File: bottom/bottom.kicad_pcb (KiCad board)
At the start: 2 copper layers, 27.5 x 37.7 mm, 2 parts, among them P1 HLW4R-2C7LF, P2 CONN_5

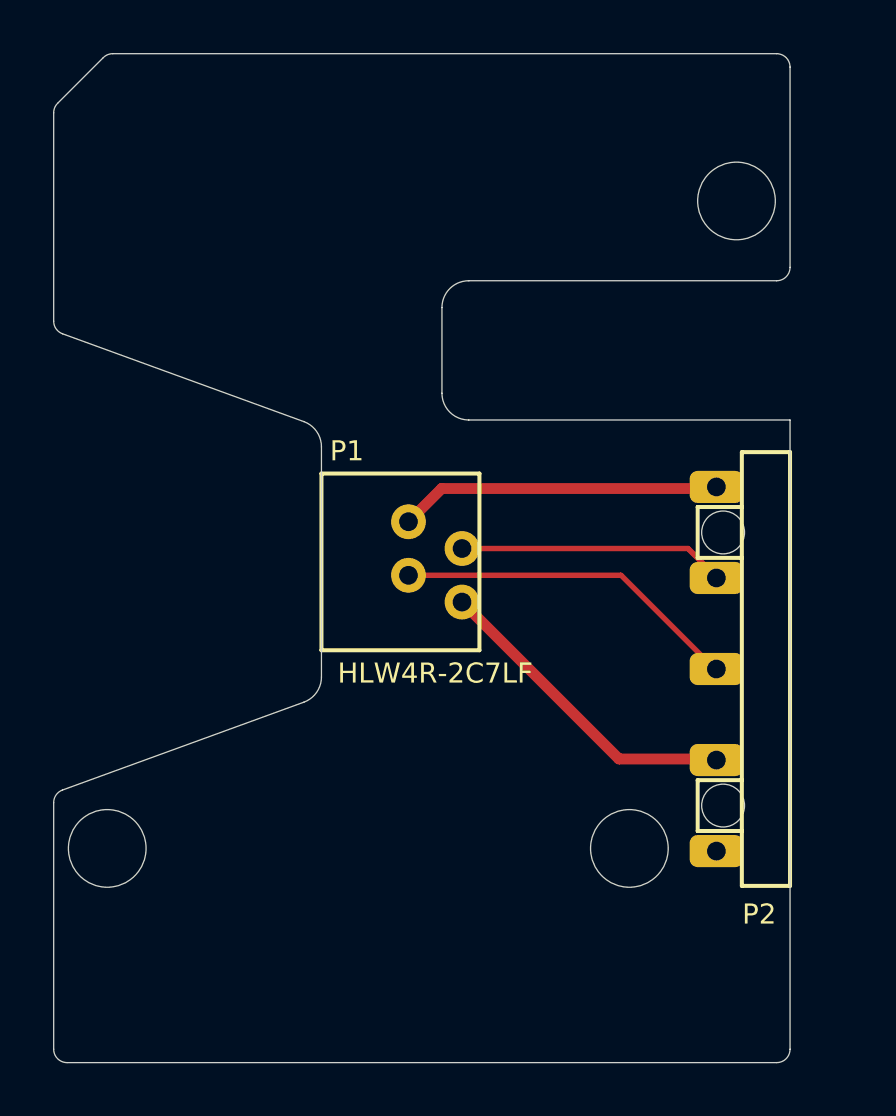
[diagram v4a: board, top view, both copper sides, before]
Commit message: Replace circles with holes.
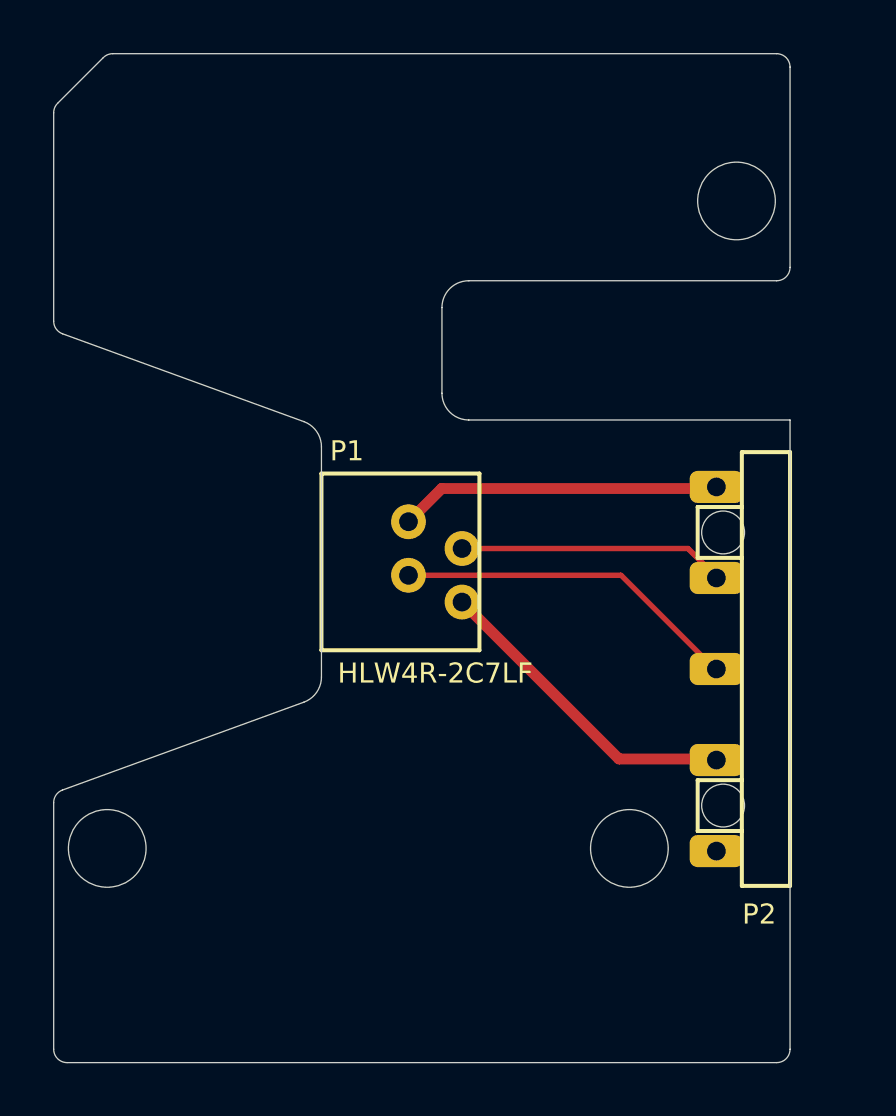
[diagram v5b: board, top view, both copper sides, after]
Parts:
- added ?: , UGL:hole_2.8999999999999773mm, Edge.Cuts at (219.3, 149.8)
- added ?: , UGL:hole_2.8999999999999773mm, Edge.Cuts at (199.8, 149.8)
- added ?: , UGL:hole_2.9000000000000057mm, Edge.Cuts at (223.3, 125.7)
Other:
- outline, holes or cut-outs redrawn
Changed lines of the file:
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@@
   )
   (gr_circle (center 219.35 149.839996) (end 221 149.839996) (layer Eco1.User) (width 0.01))
-  (gr_circle (center 219.35 149.839996) (end 219.35 151.289996) (layer Edge.Cuts) (width 0.01))
+  (module UGL:hole_2.8999999999999773mm locked (layer Edge.Cuts)
+    (at 219.35 149.839996)
+    (attr virtual)
+    (pad "" np_thru_hole circle (at 0 0) (size 2.8999999999999773 2.8999999999999773) (drill 2.8999999999999773) (layers *.Cu *.Mask F.SilkS)
+      (clearance 0.00001)
+    )
+  )
   (gr_circle (center 199.85 149.839996) (end 201.5 149.839996) (layer Eco1.User) (width 0.01))
-  (gr_circle (center 199.85 149.839996) (end 199.85 151.289996) (layer Edge.Cuts) (width 0.01))
+  (module UGL:hole_2.8999999999999773mm locked (layer Edge.Cuts)
+    (at 199.85 149.839996)
+    (attr virtual)
+    (pad "" np_thru_hole circle (at 0 0) (size 2.8999999999999773 2.8999999999999773) (drill 2.8999999999999773) (layers *.Cu *.Mask F.SilkS)
+      (clearance 0.00001)
+    )
+  )
   (gr_circle (center 223.35 125.660004) (end 225 125.660004) (layer Eco1.User) (width 0.01))
-  (gr_circle (center 223.35 125.660004) (end 223.35 127.110004) (layer Edge.Cuts) (width 0.01))
+  (module UGL:hole_2.9000000000000057mm locked (layer Edge.Cuts)
+    (at 223.35 125.660004)
+    (attr virtual)
+    (pad "" np_thru_hole circle (at 0 0) (size 2.9000000000000057 2.9000000000000057) (drill 2.9000000000000057) (layers *.Cu *.Mask F.SilkS)
+      (clearance 0.00001)
+    )
+  )
   (gr_arc (start 198.35 157.339989) (end 197.85 157.34) (angle -89.98521397) (layer Edge.Cuts) (width 0.01))
   (gr_arc (start 198.349992 148.129806) (end 198.17899 147.65996) (angle -70.01492042) (layer Edge.Cuts) (width 0.01))

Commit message: Update description.
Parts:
- ? (x3): moved to F.Cu
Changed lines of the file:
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@@
   (general
     (thickness 1.6)
-    (drawings 32)
+    (drawings 29)
     (tracks 8)
     (zones 0)
-    (modules 2)
+    (modules 5)
     (nets 6)
   )
   (page A3)
   (title_block
-    (title "UHK Touchpad - Bottom")
+    (title "UHK Touchpad Module - Bottom Board")
     (rev 1.0.0)
     (company "Ultimate Gadget Laboratories Kft.")
@@
       (net 1 /VCC) (clearance 0.0762))
   )
+  (module UGL:hole_2.8999999999999773mm locked (layer F.Cu)
+    (at 219.35 149.839996)
+    (attr virtual)
+    (fp_text reference "" (at 0 0) (layer F.SilkS)
+      (effects (font (size 1.27 1.27) (thickness 0.15)))
+    )
+    (fp_text value "" (at 0 0) (layer F.SilkS)
+      (effects (font (size 1.27 1.27) (thickness 0.15)))
+    )
+    (pad "" np_thru_hole circle (at 0 0) (size 2.9 2.9) (drill 2.9) (layers *.Cu *.Mask F.SilkS)
+      (clearance 0.00001))
+  )
+  (module UGL:hole_2.8999999999999773mm locked (layer F.Cu)
+    (at 199.85 149.839996)
+    (attr virtual)
+    (fp_text reference "" (at 0 0) (layer F.SilkS)
+      (effects (font (size 1.27 1.27) (thickness 0.15)))
+    )
+    (fp_text value "" (at 0 0) (layer F.SilkS)
+      (effects (font (size 1.27 1.27) (thickness 0.15)))
+    )
+    (pad "" np_thru_hole circle (at 0 0) (size 2.9 2.9) (drill 2.9) (layers *.Cu *.Mask F.SilkS)
+      (clearance 0.00001))
+  )
+  (module UGL:hole_2.9000000000000057mm locked (layer F.Cu)
+    (at 223.35 125.660004)
+    (attr virtual)
+    (fp_text reference "" (at 0 0) (layer F.SilkS)
+      (effects (font (size 1.27 1.27) (thickness 0.15)))
+    )
+    (fp_text value "" (at 0 0) (layer F.SilkS)
+      (effects (font (size 1.27 1.27) (thickness 0.15)))
+    )
+    (pad "" np_thru_hole circle (at 0 0) (size 2.9 2.9) (drill 2.9) (layers *.Cu *.Mask F.SilkS)
+      (clearance 0.00001))
+  )
   (gr_text "PCB ID: touchpad_bottom_1.0.0" (at 212 156.8) (layer B.SilkS)
     (effects (font (size 0.75 0.75) (thickness 0.15)) (justify mirror))
   )
   (gr_circle (center 219.35 149.839996) (end 221 149.839996) (layer Eco1.User) (width 0.01))
-  (module UGL:hole_2.8999999999999773mm locked (layer Edge.Cuts)
-    (at 219.35 149.839996)
-    (attr virtual)
-    (pad "" np_thru_hole circle (at 0 0) (size 2.8999999999999773 2.8999999999999773) (drill 2.8999999999999773) (layers *.Cu *.Mask F.SilkS)
-      (clearance 0.00001)
-    )
-  )
   (gr_circle (center 199.85 149.839996) (end 201.5 149.839996) (layer Eco1.User) (width 0.01))
-  (module UGL:hole_2.8999999999999773mm locked (layer Edge.Cuts)
-    (at 199.85 149.839996)
-    (attr virtual)
-    (pad "" np_thru_hole circle (at 0 0) (size 2.8999999999999773 2.8999999999999773) (drill 2.8999999999999773) (layers *.Cu *.Mask F.SilkS)
-      (clearance 0.00001)
-    )
-  )
   (gr_circle (center 223.35 125.660004) (end 225 125.660004) (layer Eco1.User) (width 0.01))
-  (module UGL:hole_2.9000000000000057mm locked (layer Edge.Cuts)
-    (at 223.35 125.660004)
-    (attr virtual)
-    (pad "" np_thru_hole circle (at 0 0) (size 2.9000000000000057 2.9000000000000057) (drill 2.9000000000000057) (layers *.Cu *.Mask F.SilkS)
-      (clearance 0.00001)
-    )
-  )
   (gr_arc (start 198.35 157.339989) (end 197.85 157.34) (angle -89.98521397) (layer Edge.Cuts) (width 0.01))
   (gr_arc (start 198.349992 148.129806) (end 198.17899 147.65996) (angle -70.01492042) (layer Edge.Cuts) (width 0.01))

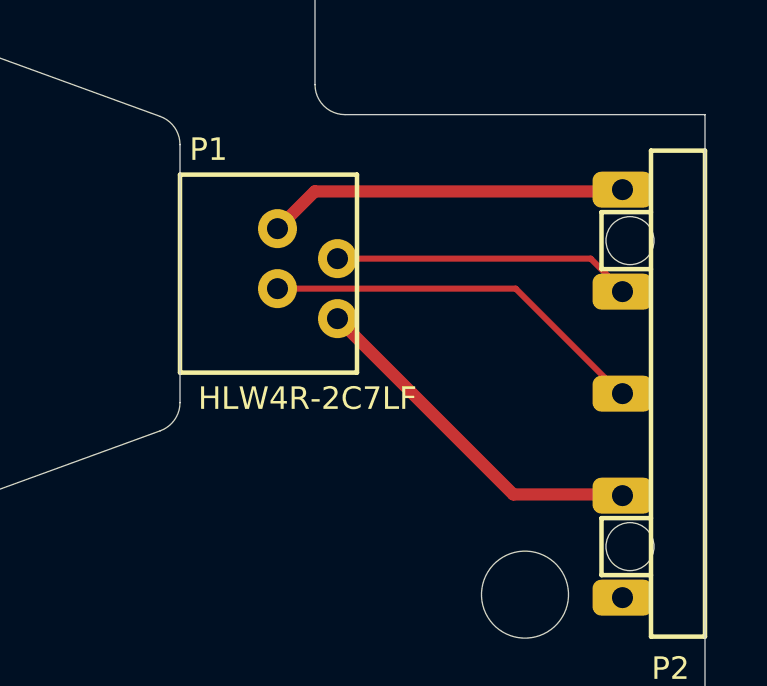
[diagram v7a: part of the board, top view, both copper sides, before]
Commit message: Increase track width on bottom PCB.
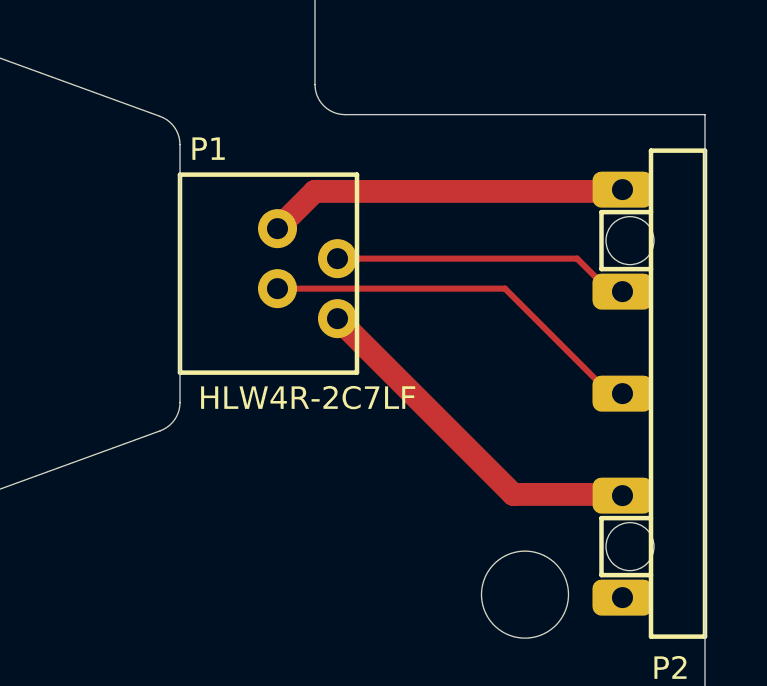
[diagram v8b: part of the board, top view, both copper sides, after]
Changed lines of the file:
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@@
-(kicad_pcb (version 20171130) (host pcbnew 5.1.2-f72e74a~84~ubuntu18.04.1)
+(kicad_pcb (version 20171130) (host pcbnew "(5.0.0)")
   (general
     (thickness 1.6)
     (drawings 33)
-    (tracks 8)
+    (tracks 10)
     (zones 0)
     (modules 5)
@@
   )
   (setup
-    (last_trace_width 0.2032)
+    (last_trace_width 0.4064)
     (user_trace_width 0.4064)
     (trace_clearance 0.2032)
@@
     (zone_45_only no)
     (trace_min 0.2032)
+    (segment_width 0.2)
+    (edge_width 0.1)
     (via_size 0.889)
     (via_drill 0.635)
@@
     (uvia_min_size 0.508)
     (uvia_min_drill 0.127)
-    (edge_width 0.1)
-    (segment_width 0.2)
     (pcb_text_width 0.3)
     (pcb_text_size 1.5 1.5)
@@
     (pad_to_mask_clearance 0)
     (aux_axis_origin 0 0)
-    (visible_elements FFFFEF7F)
+    (visible_elements 7FFFFFFF)
     (pcbplotparams
       (layerselection 0x00030_ffffffff)
@@
     (uvia_dia 0.508)
     (uvia_drill 0.127)
+    (diff_pair_gap 0.25)
     (diff_pair_width 0.2032)
-    (diff_pair_gap 0.25)
     (add_net /GND)
     (add_net /MERGE_SENSE)
@@
   (gr_circle (center 223.35 155.339996) (end 223.35 157.239996) (layer Eco1.User) (width 0.01))
   (gr_arc (start 199.666942 155.331772) (end 197.85 155.948276) (angle -322.8371138) (layer Eco1.User) (width 0.01))
-  (segment (start 211.1 137.639999) (end 212.339999 136.4) (width 0.4064) (layer F.Cu) (net 1))
-  (segment (start 212.339999 136.4) (end 222.6 136.4) (width 0.4064) (layer F.Cu) (net 1))
-  (segment (start 213.1 138.639999) (end 221.539999 138.639999) (width 0.2032) (layer F.Cu) (net 2))
-  (segment (start 221.539999 138.639999) (end 222.6 139.7) (width 0.2032) (layer F.Cu) (net 2))
-  (segment (start 211.1 139.639999) (end 219.039999 139.639999) (width 0.2032) (layer F.Cu) (net 3))
-  (segment (start 219.039999 139.639999) (end 222.6 143.2) (width 0.2032) (layer F.Cu) (net 3))
-  (segment (start 213.1 140.639999) (end 218.960001 146.5) (width 0.4064) (layer F.Cu) (net 4))
-  (segment (start 218.960001 146.5) (end 222.6 146.5) (width 0.4064) (layer F.Cu) (net 4))
+  (segment (start 211.1 137.639999) (end 212.339999 136.4) (width 0.762) (layer F.Cu) (net 1))
+  (segment (start 212.339999 136.4) (end 222.6 136.4) (width 0.762) (layer F.Cu) (net 1))
+  (segment (start 222.1484 139.7) (end 222.6 139.7) (width 0.2032) (layer F.Cu) (net 2))
+  (segment (start 213.1 138.639999) (end 221.088399 138.639999) (width 0.2032) (layer F.Cu) (net 2))
+  (segment (start 221.088399 138.639999) (end 222.1484 139.7) (width 0.2032) (layer F.Cu) (net 2))
+  (segment (start 222.2448 143.2) (end 222.6 143.2) (width 0.2032) (layer F.Cu) (net 3))
+  (segment (start 211.1 139.639999) (end 218.684799 139.639999) (width 0.2032) (layer F.Cu) (net 3))
+  (segment (start 218.684799 139.639999) (end 222.2448 143.2) (width 0.2032) (layer F.Cu) (net 3))
+  (segment (start 213.1 140.639999) (end 218.960001 146.5) (width 0.762) (layer F.Cu) (net 4))
+  (segment (start 218.960001 146.5) (end 222.6 146.5) (width 0.762) (layer F.Cu) (net 4))
 )
